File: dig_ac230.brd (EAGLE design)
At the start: 100 x 85 mm, 134 parts, among them IC1 74HC595D, IC101 ATMEGA32A-AU, IC102 DS1337S, IC103 MAX487CSA, IC104 74HC166D, IC2 LTV-356T, IC3 LTV-356T, IC4 LTV-356T, IC5 LTV-356T, IC6 LTV-356T, IC7 LTV-356T, IC8 LTV-356T, IC9 LTV-356T, K301 S202S02, K302 S202S02, K303 S202S02, K304 S202S02, K305 S202S02, K306 S202S02, K307 S202S02, K308 S202S02, Q1 32,768kHz, Q2 BCR191, Q3 BCR191, Q4 BCR191, Q5 BCR191, Q6 BCR191, Q7 BCR191, Q8 BCR191, Q9 BCR191, X1 RIA-73-02, X10 RIA-73-02, X11 RIA-73-02, X12 RIA-73-02, X2 RIA-73-02, X3 RIA-73-02, X4 RIA-73-02, X5 RIA-73-02, X6 RIA-73-02, X7 RIA-73-02, X8 RIA-73-02, X9 RIA-73-02

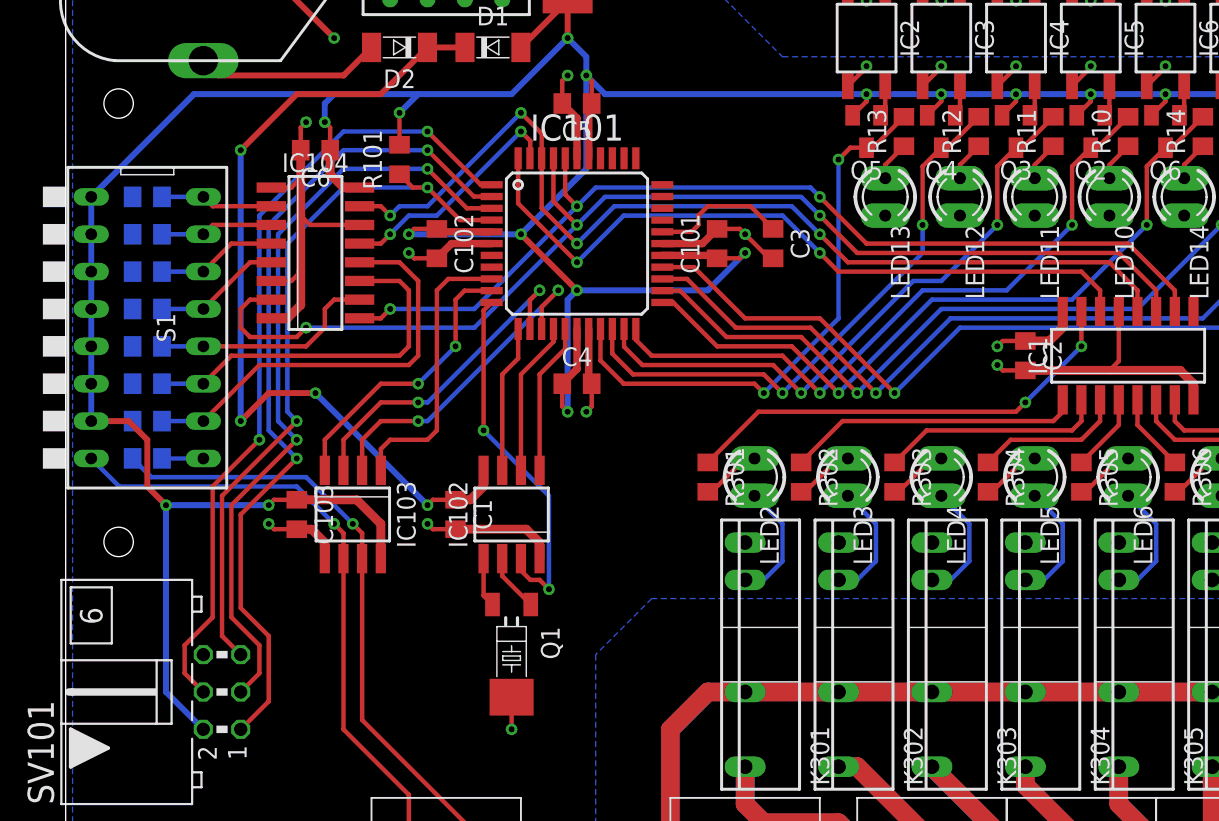
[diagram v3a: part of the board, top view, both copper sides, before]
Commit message: Leiterbahnführung verbessert; Analog ground verbessert
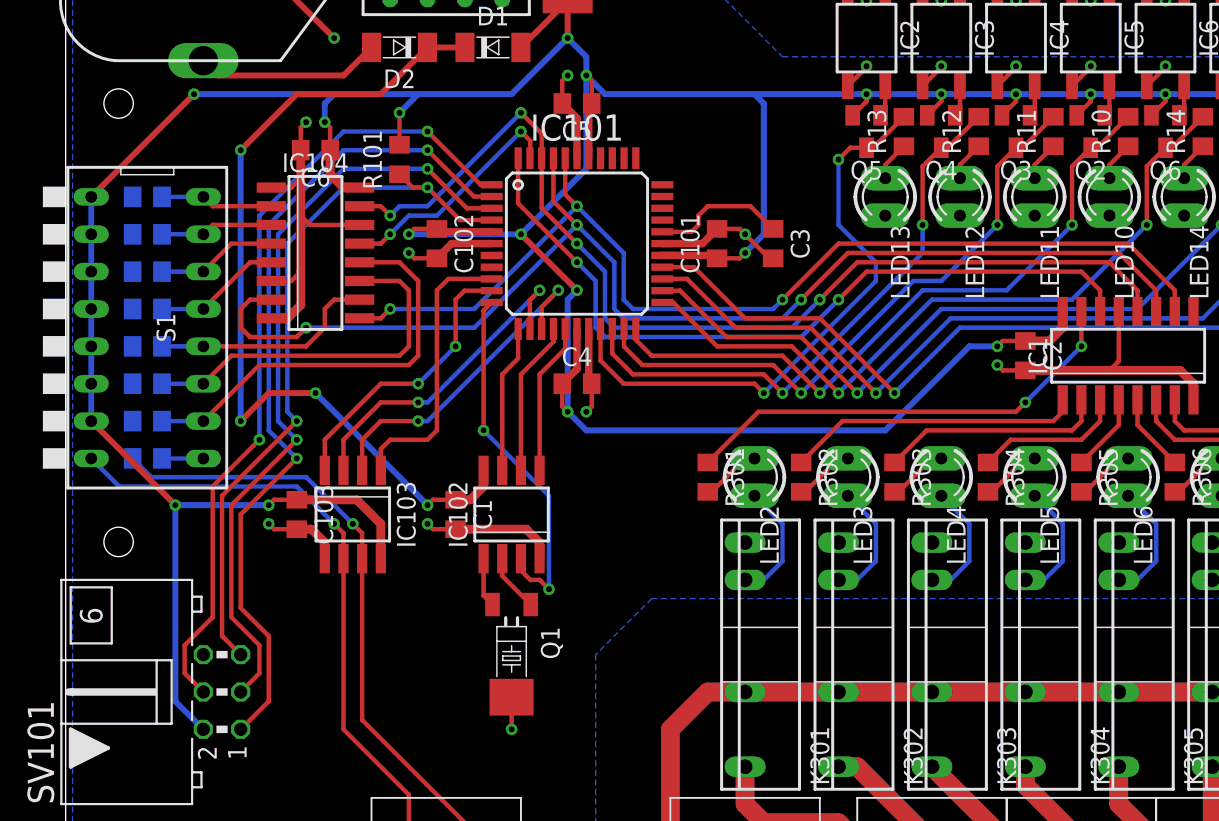
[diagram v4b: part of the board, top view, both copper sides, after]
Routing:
- net +5V: track 279.3 -> 308.4 mm, vias 20 -> 21
- net !R: track 67.0 -> 71.5 mm
- net C1: track 79.3 -> 83.3 mm
- net C2: track 67.6 -> 71.0 mm
- net DO: track 49.2 -> 52.1 mm
- net IN0: track 37.8 -> 39.9 mm

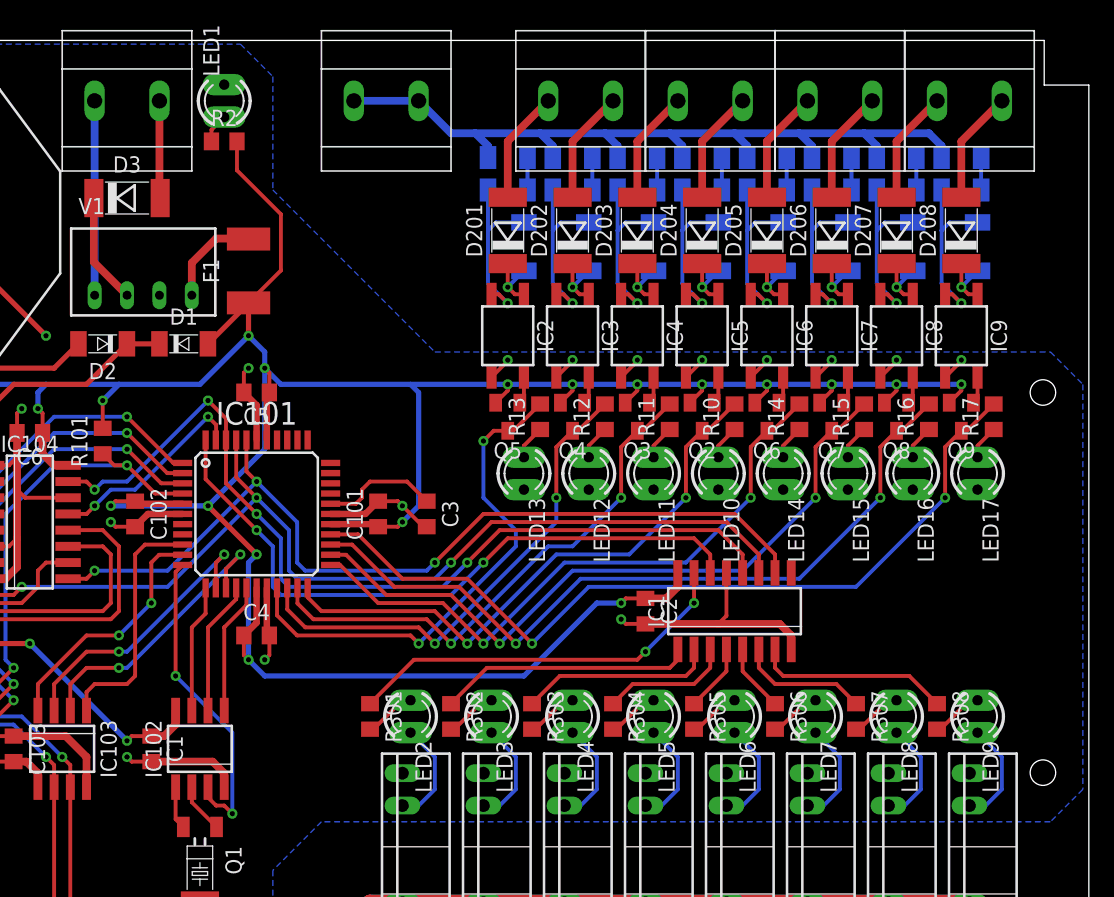
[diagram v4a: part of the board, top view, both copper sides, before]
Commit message: Statusleds, Temperatur- und Batteriemessung hinzugefügt
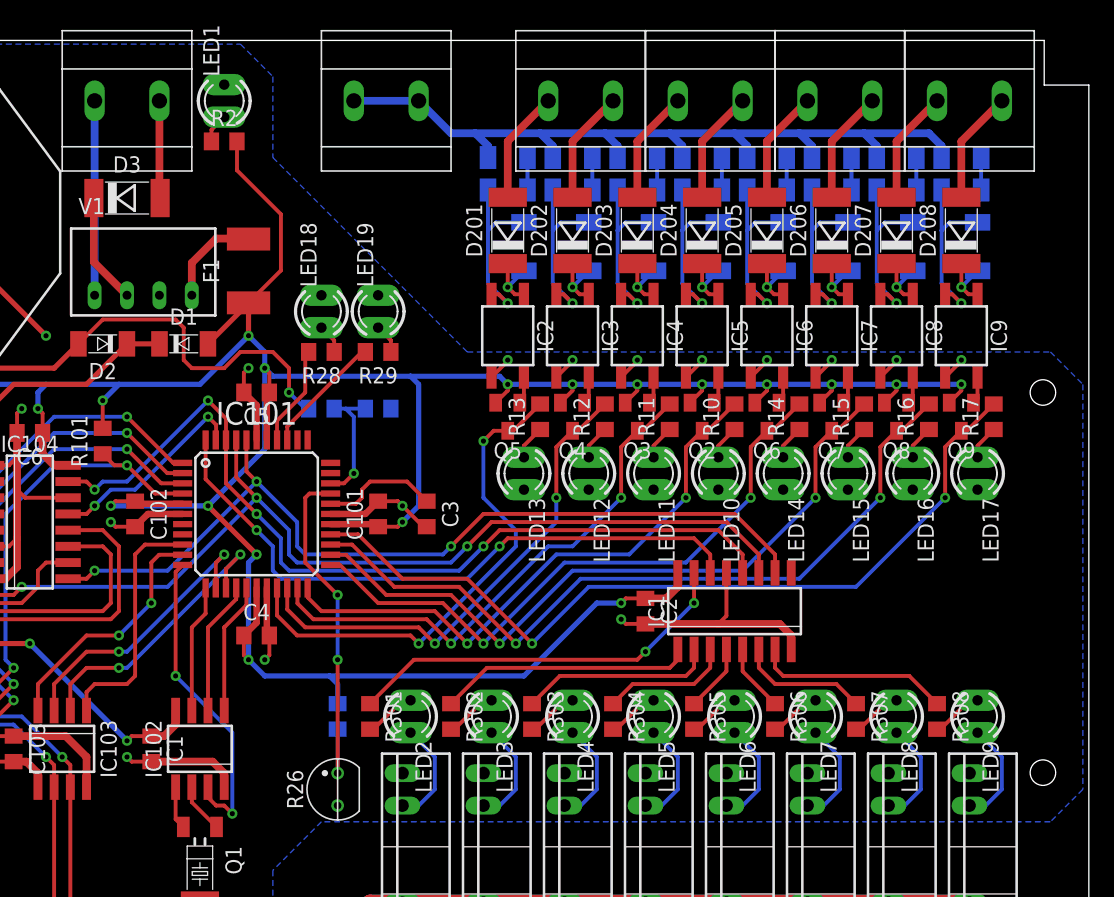
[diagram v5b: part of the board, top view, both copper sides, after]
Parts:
- added LED18: GN, led:LED3MM
- added LED19: RT, led:LED3MM
- added R26: KTY81-210, sensor:TO92
- added R27: 3,3kΩ, passiv:CHIP_0805
- added R28, R29: 390Ω, passiv:CHIP_0805
- added R30, R31: 1MΩ, passiv:CHIP_0805
- LED1, LED10, LED11, LED12, LED13, LED14, LED15, LED16, LED17, LED2, LED3, LED4, LED5, LED6, LED7, LED8, LED9: value (none) -> GN
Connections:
- new net BAT: IC101.31, R30.1, R31.2
- new net N$61: IC101.30, R26.1, R27.1
- new net N$62: LED18.A, R28.1
- new net N$63: LED19.A, R29.1
- new net N$90: IC101.37, R28.2
- new net N$92: IC101.36, R29.2
- net +5V: now also R27.2
- net GND: now also LED18.K, LED19.K, R26.2, R31.1
- net N$21: now also R30.2
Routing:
- net N$61: track 0.00 -> 28.2 mm, vias 0 -> 2
- net N$21: track 12.6 -> 38.0 mm, vias 0 -> 1
- net BAT: track 0.00 -> 9.93 mm, vias 0 -> 1
- net N$92: track 0.00 -> 9.60 mm
- net N$90: track 0.00 -> 7.93 mm
- net +5V: track 308.4 -> 311.5 mm
- net N$63: track 0.00 -> 2.32 mm
- net N$62: track 0.00 -> 2.32 mm
- net C1: track 83.3 -> 81.5 mm
- net !R: track 71.5 -> 69.7 mm
- net DO: track 52.1 -> 50.3 mm
- net C2: track 71.0 -> 69.2 mm

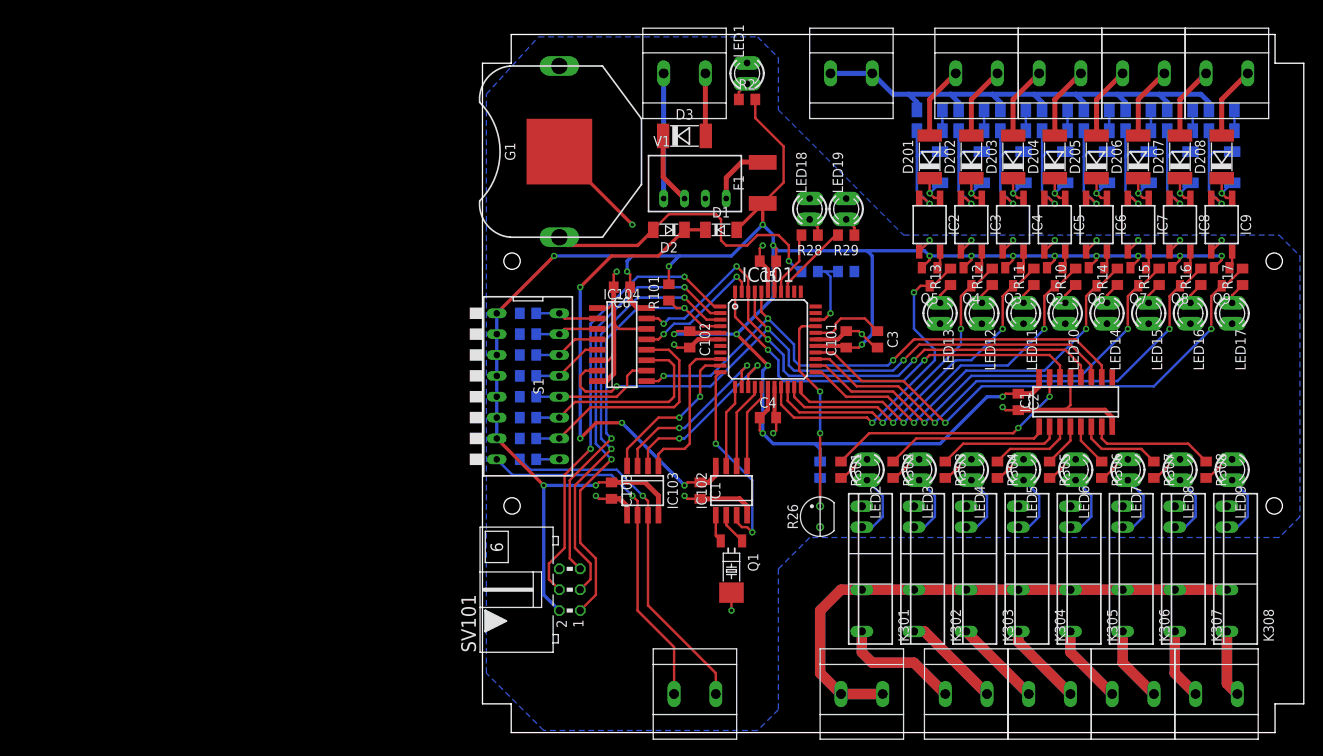
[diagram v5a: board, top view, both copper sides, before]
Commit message: Halbleiterrelais wegen gehäuse versetzt
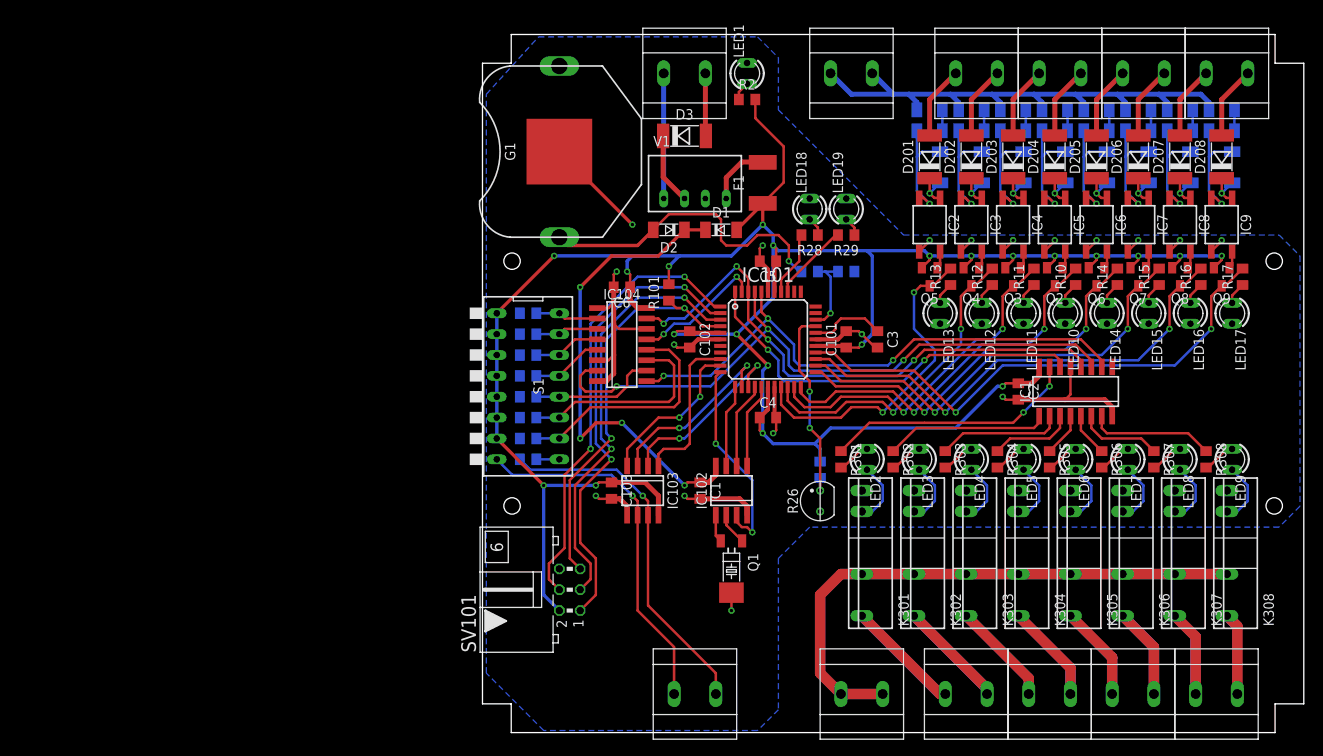
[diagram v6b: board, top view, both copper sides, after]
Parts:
- moved K301 1.91 mm to (48.3, 22.2)
- moved K302 1.91 mm to (54.6, 22.2)
- moved K303 1.91 mm to (61.0, 22.2)
- moved K304 1.91 mm to (67.3, 22.2)
- moved K305 1.91 mm to (73.7, 22.2)
- moved K306 1.91 mm to (80.0, 22.2)
- moved K307 1.91 mm to (86.4, 22.2)
- moved K308 1.91 mm to (92.7, 22.2)
- moved R26 1.90 mm to (43.2, 28.6)
- moved LED2 1.27 mm to (48.9, 33.7)
- moved LED3 1.27 mm to (55.2, 33.7)
- moved LED4 1.27 mm to (61.6, 33.7)
- moved LED5 1.27 mm to (67.9, 33.7)
- moved LED6 1.27 mm to (74.3, 33.7)
- moved LED7 1.27 mm to (80.6, 33.7)
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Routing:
- net N: track 64.7 -> 71.8 mm
- net L: track 133.7 -> 137.6 mm
- net N$74: track 21.6 -> 25.4 mm
- net N$89: track 16.3 -> 20.1 mm
- net N$84: track 17.3 -> 21.2 mm
- net N$82: track 18.4 -> 22.2 mm
- net N$78: track 19.4 -> 23.3 mm
- net N$76: track 20.5 -> 24.3 mm
- net N$61: track 28.2 -> 24.4 mm
- net N$72: track 24.1 -> 26.4 mm
- net N$68: track 29.6 -> 28.2 mm
- net IN7: track 65.6 -> 64.6 mm
- net IN6: track 60.2 -> 59.2 mm
- net IN5: track 54.8 -> 53.8 mm
- net IN4: track 49.4 -> 48.4 mm
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
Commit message: Schematik übersichtlicher gemacht; Bauteile neu benannt; Werte ergänzt
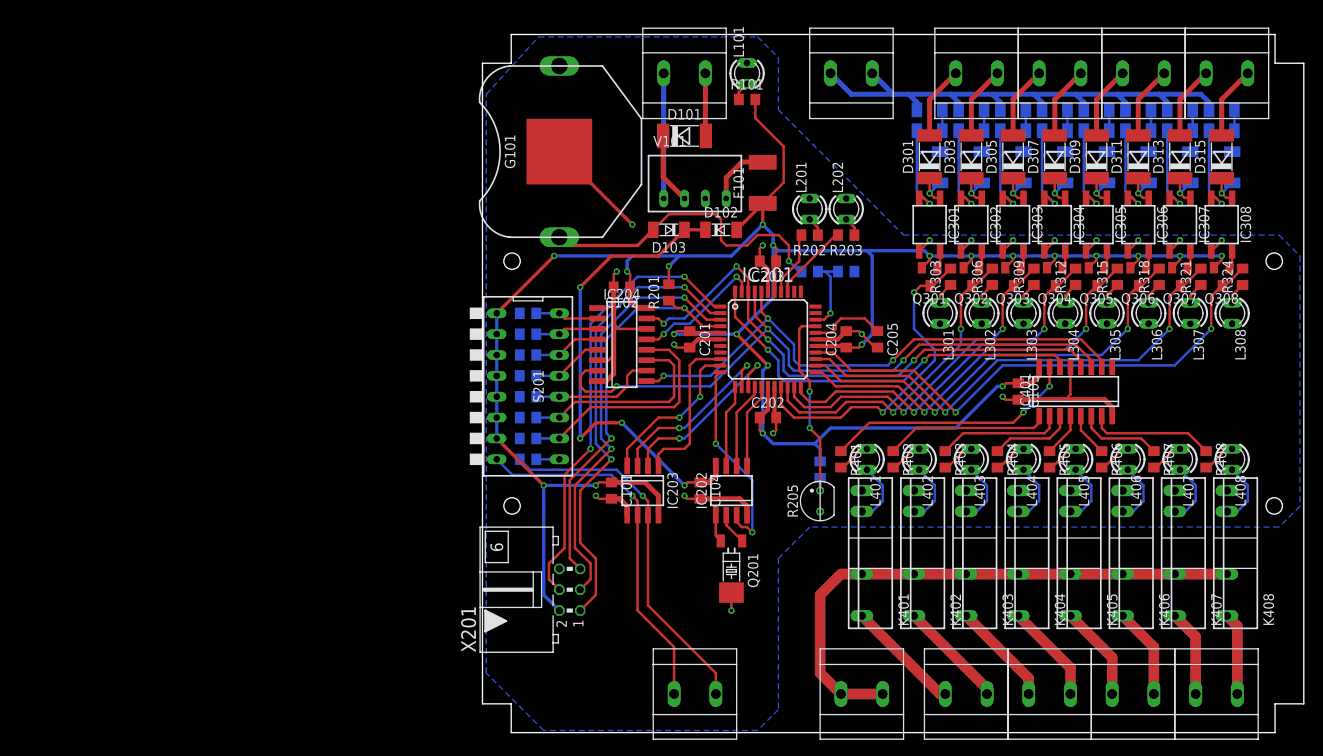
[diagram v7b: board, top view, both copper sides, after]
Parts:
- removed C2, C6: 100nF, passiv:CHIP_0805
- removed R1: 120Ω, passiv:CHIP_0805
- removed R12, R13, R2, R28, R29: 390Ω, passiv:CHIP_0805
- removed R18, R19, R20: 120kΩ, passiv:CHIP_1206
- removed R26: KTY81-210, sensor:TO92
- removed R27: 3,3kΩ, passiv:CHIP_0805
- removed R3, R4: (no value), passiv:CHIP_0805
- added C201, C204: 100nF, passiv:CHIP_0805
- added R310, R313, R316, R319, R322: 120kΩ, passiv:CHIP_1206
- added R401, R402, R403, R404, R405, R406, R407, R408: 180Ω, passiv:CHIP_0805
- D101: value (none) -> TMBAT49
- R101: value 10k -> 390Ω
- R201: value 120kΩ -> 10k; device passiv:CHIP_1206 -> passiv:CHIP_0805
- R202, R203: value 120kΩ -> 390Ω; device passiv:CHIP_1206 -> passiv:CHIP_0805
- R204: value 120kΩ -> 3,3kΩ; device passiv:CHIP_1206 -> passiv:CHIP_0805
- R205: value 120kΩ -> KTY81-210; device passiv:CHIP_1206 -> sensor:TO92
- R206: value 120kΩ -> 120Ω; device passiv:CHIP_1206 -> passiv:CHIP_0805
- R207, R208: value 120kΩ -> 22kΩ; device passiv:CHIP_1206 -> passiv:CHIP_0805
- R209, R210, R211, R212, R213: value (none) -> 22kΩ
- R301, R302, R304, R305, R307, R308: value 180Ω -> 120kΩ; device passiv:CHIP_0805 -> passiv:CHIP_1206
- R303, R306: value 180Ω -> 390Ω
- X201: value (none) -> ISP
- moved R208 88.0 mm to (7.62, 48.9), turned to 180 degrees
- moved R206 84.4 mm to (7.62, 33.7), turned to 180 degrees
- moved R207 82.4 mm to (7.62, 51.4), turned to 180 degrees
- moved R205 56.3 mm to (43.2, 28.6), flipped to the top, turned to 90 degrees
- moved C103 51.0 mm to (67.3, 41.9)
- moved R204 50.2 mm to (43.2, 32.4), turned to 90 degrees
- moved R308 48.6 mm to (66.7, 76.2), flipped to the bottom, turned to 180 degrees
- moved R305 43.6 mm to (61.6, 76.2), flipped to the bottom, turned to 180 degrees
- moved R307 43.5 mm to (66.7, 73.7), flipped to the bottom, turned to 0 degrees
- moved R302 42.8 mm to (56.5, 76.2), flipped to the bottom, turned to 180 degrees
- moved R301 41.4 mm to (56.5, 73.7), flipped to the bottom, turned to 0 degrees
- moved R304 40.1 mm to (61.6, 73.7), flipped to the bottom, turned to 0 degrees
- moved R201 37.4 mm to (24.8, 54.0), flipped to the top, turned to 90 degrees
- moved C101 34.0 mm to (17.8, 29.8), turned to 270 degrees
- moved R306 25.9 mm to (64.1, 55.9), turned to 90 degrees
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- renumbered C1 to C104, C3 to C205, C4 to C202, C5 to C203, D1 to D102, D10 to D314, D11 to D316, D2 to D103, D201 to D301, D202 to D303, D203 to D305, D204 to D307, D205 to D309, D206 to D311, D207 to D313, D208 to D315, D3 to D101, D4 to D302, D5 to D304, D6 to D306, D7 to D308, D8 to D310, D9 to D312, F1 to F101, G1 to G101, IC1 to IC401, IC101 to IC201, IC102 to IC202, IC103 to IC203, IC104 to IC204, IC2 to IC301, IC3 to IC302, IC4 to IC303, IC5 to IC304, IC6 to IC305, IC7 to IC306, IC8 to IC307, IC9 to IC308, K301 to K401, K302 to K402, K303 to K403, K304 to K404, K305 to K405, K306 to K406, K307 to K407, K308 to K408, LED1 to L101, LED10 to L304, LED11 to L303, LED12 to L302, LED13 to L301, LED14 to L305, LED15 to L306, LED16 to L307, LED17 to L308, LED18 to L201, LED19 to L202, LED2 to L401, LED3 to L402, LED4 to L403, LED5 to L404, LED6 to L405, LED7 to L406, LED8 to L407, LED9 to L408, Q1 to Q201, Q2 to Q304, Q3 to Q303, Q4 to Q302, Q5 to Q301, Q6 to Q305, Q7 to Q306, Q8 to Q307, Q9 to Q308, R10 to R312, R11 to R309, R14 to R315, R15 to R318, R16 to R321, R17 to R324, R21 to R311, R22 to R314, R23 to R317, R24 to R320, R25 to R323, R30 to R102, R31 to R103, R5 to R209, R6 to R210, R7 to R211, R8 to R212, R9 to R213, S1 to S201, SV101 to X201, V1 to V101, X1 to X101, X10 to X404, X11 to X405, X12 to X401, X2 to X202, X3 to X302, X4 to X303, X5 to X304, X6 to X305, X7 to X301, X8 to X402, X9 to X403
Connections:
- net VCC renamed N$64
- net +5V: now also C201.1, C204.1, R201.2, R204.2; no longer C2.1, C6.1, R2.2, R27.2
- net GND: now also C201.2, C204.2, R205.2, R207.1, R208.1; no longer C2.2, C6.2, R26.2, R3.1, R4.1
- net IN0: now also R303.2; no longer R13.2
- net IN1: now also R306.2; no longer R12.2
- net N: now also R302.1, R305.1, R308.1; no longer R18.1, R19.1, R20.1
- net N$10: now also R313.2; no longer R205.2
- net N$103: now also R401.2; no longer R301.2
- net N$104: now also R402.2; no longer R302.2
- net N$105: now also R403.2; no longer R303.2
- net N$106: now also R404.2; no longer R304.2
- net N$107: now also R405.2; no longer R305.2
- net N$108: now also R406.2; no longer R306.2
- net N$109: now also R407.2; no longer R307.2
- net N$110: now also R408.2; no longer R308.2
- net N$12: now also R316.2; no longer R206.2
- net N$14: now also R319.2; no longer R207.2
- net N$16: now also R322.2; no longer R208.2
- net N$2: now also R301.2; no longer R201.2
- net N$22: now also R206.1; no longer R1.1
- net N$26: now also R207.2; no longer R3.2
- net N$27: now also R208.2; no longer R4.2
- net N$33: now also R206.2; no longer R1.2
- net N$35: now also R301.1, R302.2; no longer R18.2, R201.1
- net N$37: now also R304.1, R305.2; no longer R19.2, R202.1
- net N$38: now also R306.1; no longer R12.1
- net N$39: now also R307.1, R308.2; no longer R20.2, R203.1
- net N$4: now also R304.2; no longer R202.2
- net N$40: now also R303.1; no longer R13.1
- net N$42: now also R201.1; no longer R101.1
- net N$44: now also R101.1; no longer R2.1
- net N$50: now also R310.1; no longer R204.1
- net N$51: now also R401.1; no longer R301.1
- net N$53: now also R402.1; no longer R302.1
- net N$54: now also R403.1; no longer R303.1
- net N$56: now also R404.1; no longer R304.1
- net N$57: now also R313.1; no longer R205.1
- net N$58: now also R405.1; no longer R305.1
- net N$59: now also R406.1; no longer R306.1
- net N$6: now also R307.2; no longer R203.2
- net N$60: now also R407.1; no longer R307.1
- net N$61: now also R204.1, R205.1; no longer R26.1, R27.1
- net N$62: now also R202.1; no longer R28.1
- net N$63: now also R203.1; no longer R29.1
- net N$66: now also R408.1; no longer R308.1
- net N$67: now also R316.1; no longer R206.1
- net N$71: now also R319.1; no longer R207.1
- net N$79: now also R322.1; no longer R208.1
- net N$8: now also R310.2; no longer R204.2
- net N$90: now also R202.2; no longer R28.2
- net N$92: now also R203.2; no longer R29.2
